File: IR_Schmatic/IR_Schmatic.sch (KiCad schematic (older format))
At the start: 8 parts

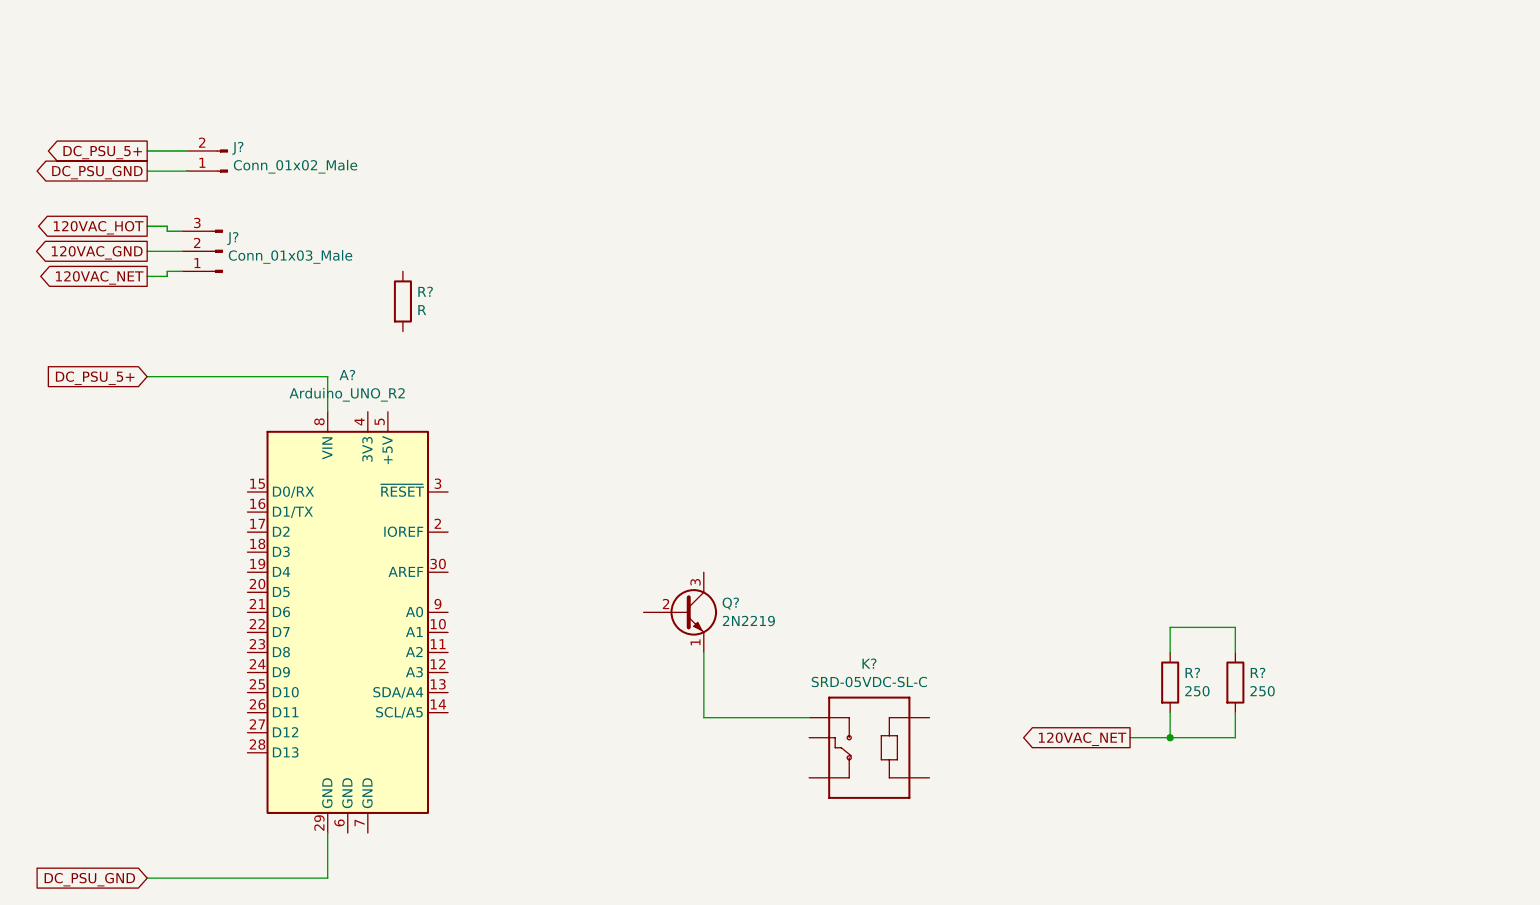
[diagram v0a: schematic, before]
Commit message: Add proper relay
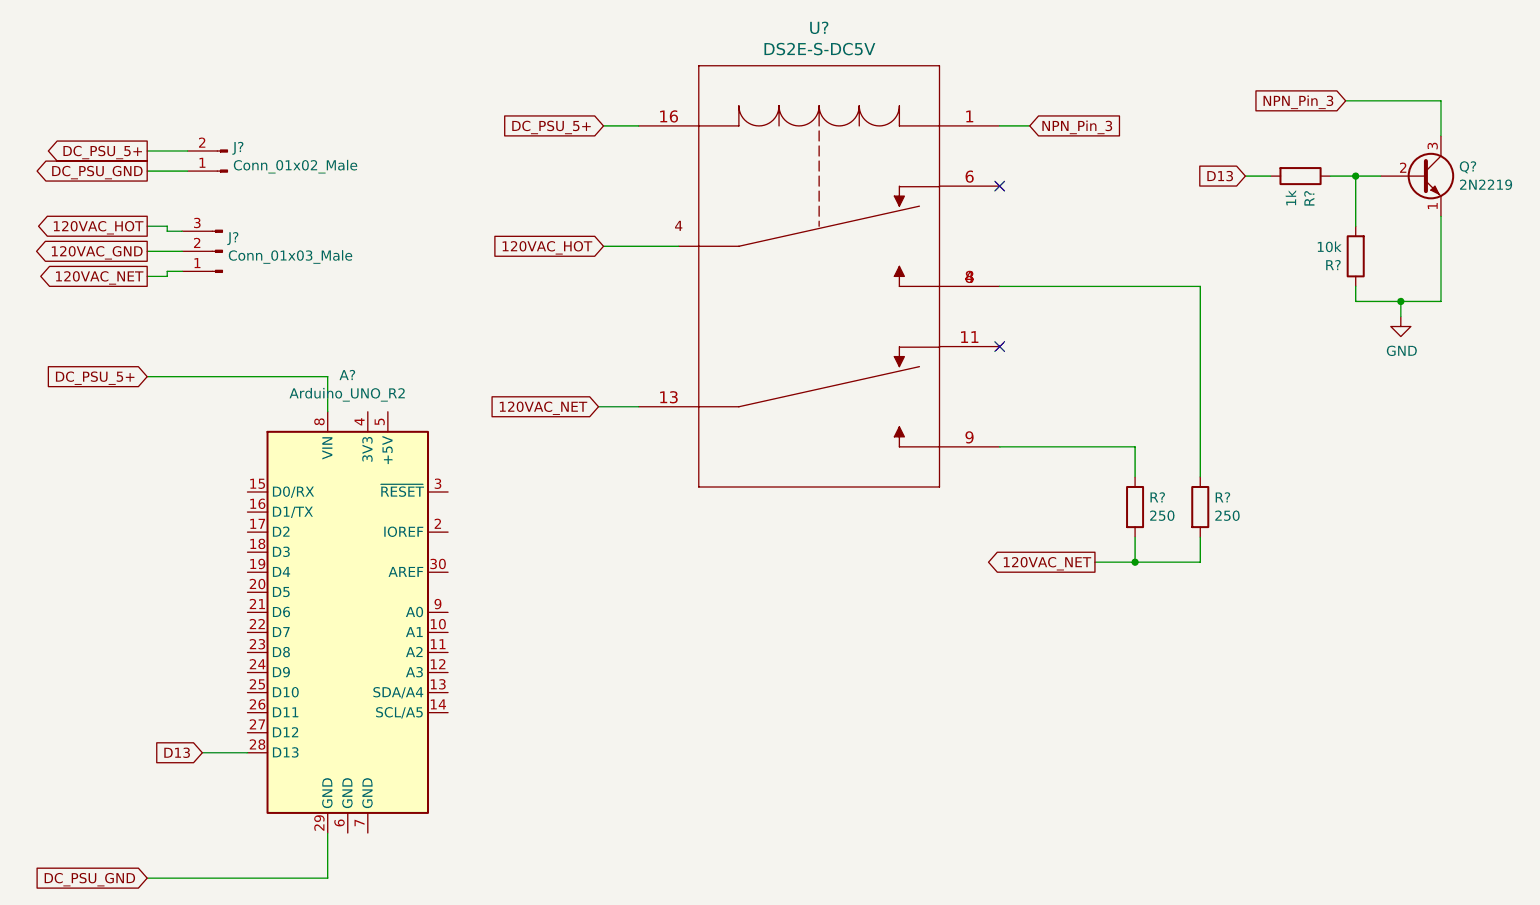
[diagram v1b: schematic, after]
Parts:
- removed K?: SRD-05VDC-SL-C, RELAY_SRD-05VDC-SL-C, symbol SRD-05VDC-SL-C:SRD-05VDC-SL-C
- added R?: 10k, symbol Device:R
- added U?: DS2E-S-DC5V, RELAY_DS2E_PAN, symbol 2020-05-14_18-57-15:DS2E-S-DC5V
- R?: value R -> 1k
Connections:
- net 120VAC_HOT: now also U?.~
- net 120VAC_NET: now also U?.13
- net DC_PSU_5+: now also U?.16
- net D13: now reaches A?.28 (D13)
- net D13: now also R?.2
- net GND: now reaches Q?.1 (E)
- net GND: now also R?.1
- net at Q?.2 (B): now also R?.1, R?.2
- net NPN_Pin_3: now reaches Q?.3 (C)
- net NPN_Pin_3: now also U?.1
- net at R?.1: now also U?.4, U?.8; no longer R?.1
- new net: R?.1, U?.9
- no-connect marks 0 -> 2
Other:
- moved on the sheet: Q?, R?
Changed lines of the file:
@@
 120VAC_NET
-$Comp
-L SRD-05VDC-SL-C:SRD-05VDC-SL-C K?
-U 1 1 5EBC6DD9
-P 5850 4300
-F 0 "K?" H 5850 4667 50  0000 C CNN
-F 1 "SRD-05VDC-SL-C" H 5850 4576 50  0000 C CNN
-F 2 "RELAY_SRD-05VDC-SL-C" H 5850 4300 50  0001 L BNN
-F 3 "SONGLE RELAY" H 5850 4300 50  0001 L BNN
-F 4 "IPC-7251" H 5850 4300 50  0001 L BNN "Field4"
-	1    5850 4300
-	-1   0    0    -1
-$EndComp
 $Comp
 L Transistor_BJT:2N2219 Q?
 U 1 1 5EBCC234
-P 4925 3675
-F 0 "Q?" H 5115 3721 50  0000 L CNN
-F 1 "2N2219" H 5115 3630 50  0000 L CNN
-F 2 "Package_TO_SOT_THT:TO-39-3" H 5125 3600 50  0001 L CIN
-F 3 "http://www.onsemi.com/pub_link/Collateral/2N2219-D.PDF" H 4925 3675 50  0001 L CNN
-	1    4925 3675
+P 8600 1500
+F 0 "Q?" H 8790 1546 50  0000 L CNN
+F 1 "2N2219" H 8790 1455 50  0000 L CNN
+F 2 "Package_TO_SOT_THT:TO-39-3" H 8800 1425 50  0001 L CIN
+F 3 "http://www.onsemi.com/pub_link/Collateral/2N2219-D.PDF" H 8600 1500 50  0001 L CNN
+	1    8600 1500
 	1    0    0    -1
 $EndComp
@@
 L Device:R R?
 U 1 1 5EBD003C
-P 3525 2125
-F 0 "R?" H 3595 2171 50  0000 L CNN
-F 1 "R" H 3595 2080 50  0000 L CNN
-F 2 "" V 3455 2125 50  0001 C CNN
-F 3 "~" H 3525 2125 50  0001 C CNN
-	1    3525 2125
-	1    0    0    -1
+P 8000 1500
+F 0 "R?" H 8070 1546 50  0000 L CNN
+F 1 "1k" H 8070 1455 50  0000 L CNN
+F 2 "" V 7930 1500 50  0001 C CNN
+F 3 "~" H 8000 1500 50  0001 C CNN
+	1    8000 1500
+	0    1    1    0
 $EndComp
 $Comp
 L Device:R R?
 U 1 1 5EBD02FE
-P 7675 4025
-F 0 "R?" H 7745 4071 50  0000 L CNN
-F 1 "250" H 7745 3980 50  0000 L CNN
-F 2 "" V 7605 4025 50  0001 C CNN
-F 3 "~" H 7675 4025 50  0001 C CNN
-	1    7675 4025
+P 7500 3150
+F 0 "R?" H 7570 3196 50  0000 L CNN
+F 1 "250" H 7570 3105 50  0000 L CNN
+F 2 "" V 7430 3150 50  0001 C CNN
+F 3 "~" H 7500 3150 50  0001 C CNN
+	1    7500 3150
 	1    0    0    -1
 $EndComp
@@
 L Device:R R?
 U 1 1 5EBD0A16
-P 7350 4025
-F 0 "R?" H 7420 4071 50  0000 L CNN
-F 1 "250" H 7420 3980 50  0000 L CNN
-F 2 "" V 7280 4025 50  0001 C CNN
-F 3 "~" H 7350 4025 50  0001 C CNN
-	1    7350 4025
+P 7175 3150
+F 0 "R?" H 7245 3196 50  0000 L CNN
+F 1 "250" H 7245 3105 50  0000 L CNN
+F 2 "" V 7105 3150 50  0001 C CNN
+F 3 "~" H 7175 3150 50  0001 C CNN
+	1    7175 3150
+	1    0    0    -1
+$EndComp
+Text GLabel 6975 3425 0    50   Output ~ 0
+120VAC_NET
+Wire Wire Line
+	6975 3425 7175 3425
+Wire Wire Line
+	7175 3425 7175 3300
+Wire Wire Line
+	7500 3300 7500 3425
+Wire Wire Line
+	7500 3425 7175 3425
+Connection ~ 7175 3425
+Wire Wire Line
+	8150 1500 8275 1500
+Text GLabel 4525 1250 0    50   Input ~ 0
+DC_PSU_5+
+Wire Wire Line
+	8700 1125 8700 1300
+$Comp
+L Device:R R?
+U 1 1 5EBE2902
+P 8275 1900
+F 0 "R?" H 8345 1946 50  0000 L CNN
+F 1 "10k" H 8345 1855 50  0000 L CNN
+F 2 "" V 8205 1900 50  0001 C CNN
+F 3 "~" H 8275 1900 50  0001 C CNN
+	1    8275 1900
+	-1   0    0    1
+$EndComp
+Wire Wire Line
+	8275 1750 8275 1500
+Connection ~ 8275 1500
+Wire Wire Line
+	8275 1500 8400 1500
+$Comp
+L power:GND #PWR?
+U 1 1 5EBE361B
+P 8500 2200
+F 0 "#PWR?" H 8500 1950 50  0001 C CNN
+F 1 "GND" H 8505 2027 50  0000 C CNN
+F 2 "" H 8500 2200 50  0001 C CNN
+F 3 "" H 8500 2200 50  0001 C CNN
+	1    8500 2200
 	1    0    0    -1
 $EndComp
 Wire Wire Line
-	5025 3875 5025 4200
+	8275 2050 8275 2125
 Wire Wire Line
-	5025 4200 5550 4200
-Text GLabel 7150 4300 0    50   Output ~ 0
+	8275 2125 8500 2125
+Wire Wire Line
+	8700 1700 8700 2125
+Wire Wire Line
+	8700 2125 8500 2125
+Connection ~ 8500 2125
+Wire Wire Line
+	8500 2125 8500 2200
+$Comp
+L 2020-05-14_18-57-15:DS2E-S-DC5V U?
+U 1 1 5EBE681A
+P 4700 1250
+F 0 "U?" H 5600 1737 60  0000 C CNN
+F 1 "DS2E-S-DC5V" H 5600 1631 60  0000 C CNN
+F 2 "RELAY_DS2E_PAN" H 5600 1590 60  0001 C CNN
+F 3 "" H 4700 1250 60  0000 C CNN
+	1    4700 1250
+	1    0    0    -1
+$EndComp
+Wire Wire Line
+	4525 1250 4700 1250
+Text GLabel 6650 1250 2    50   Input ~ 0
+NPN_Pin_3
+Wire Wire Line
+	6500 1250 6650 1250
+Text GLabel 8225 1125 0    50   Input ~ 0
+NPN_Pin_3
+Wire Wire Line
+	8225 1125 8700 1125
+Text GLabel 4525 1850 0    50   Input ~ 0
+120VAC_HOT
+Text GLabel 4500 2650 0    50   Input ~ 0
 120VAC_NET
 Wire Wire Line
-	7150 4300 7350 4300
+	4500 2650 4700 2650
 Wire Wire Line
-	7350 4300 7350 4175
+	4525 1850 4900 1850
+NoConn ~ 6500 1550
+NoConn ~ 6500 2350
+Text GLabel 2525 4375 0    50   Input ~ 0
+D13
 Wire Wire Line
-	7675 4175 7675 4300
+	2525 4375 2750 4375
+Text GLabel 7725 1500 0    50   Input ~ 0
+D13
 Wire Wire Line
-	7675 4300 7350 4300
-Connection ~ 7350 4300
+	7725 1500 7850 1500
 Wire Wire Line
-	7350 3875 7350 3750
+	6500 2850 7175 2850
 Wire Wire Line
-	7350 3750 7675 3750
+	7175 2850 7175 3000
 Wire Wire Line
-	7675 3750 7675 3875
+	6500 2050 7500 2050
+Wire Wire Line
+	7500 2050 7500 3000
 $EndSCHEMATC
